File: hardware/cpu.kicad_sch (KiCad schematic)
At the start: 9 parts, among them U1 H3

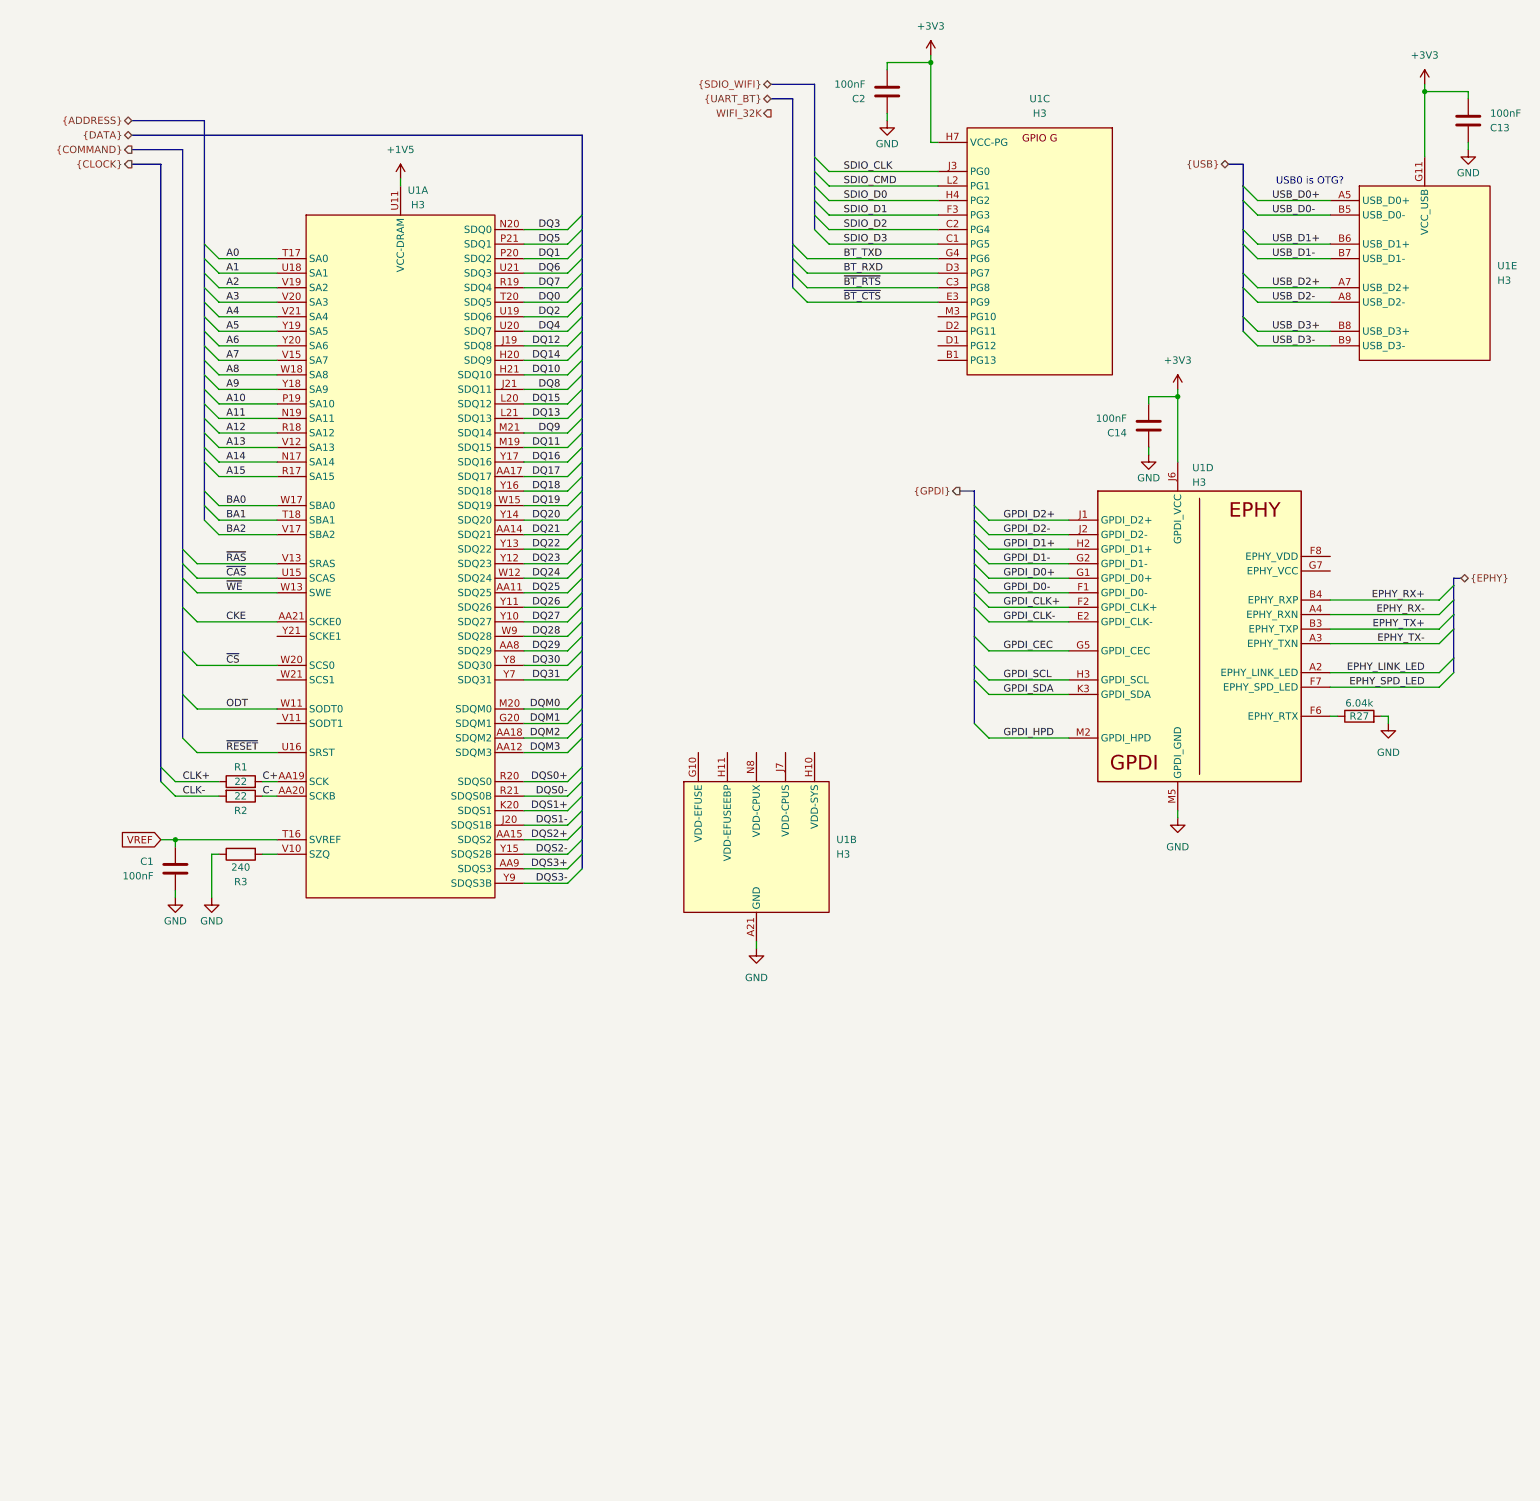
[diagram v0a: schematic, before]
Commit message: Add eMMC and uSD
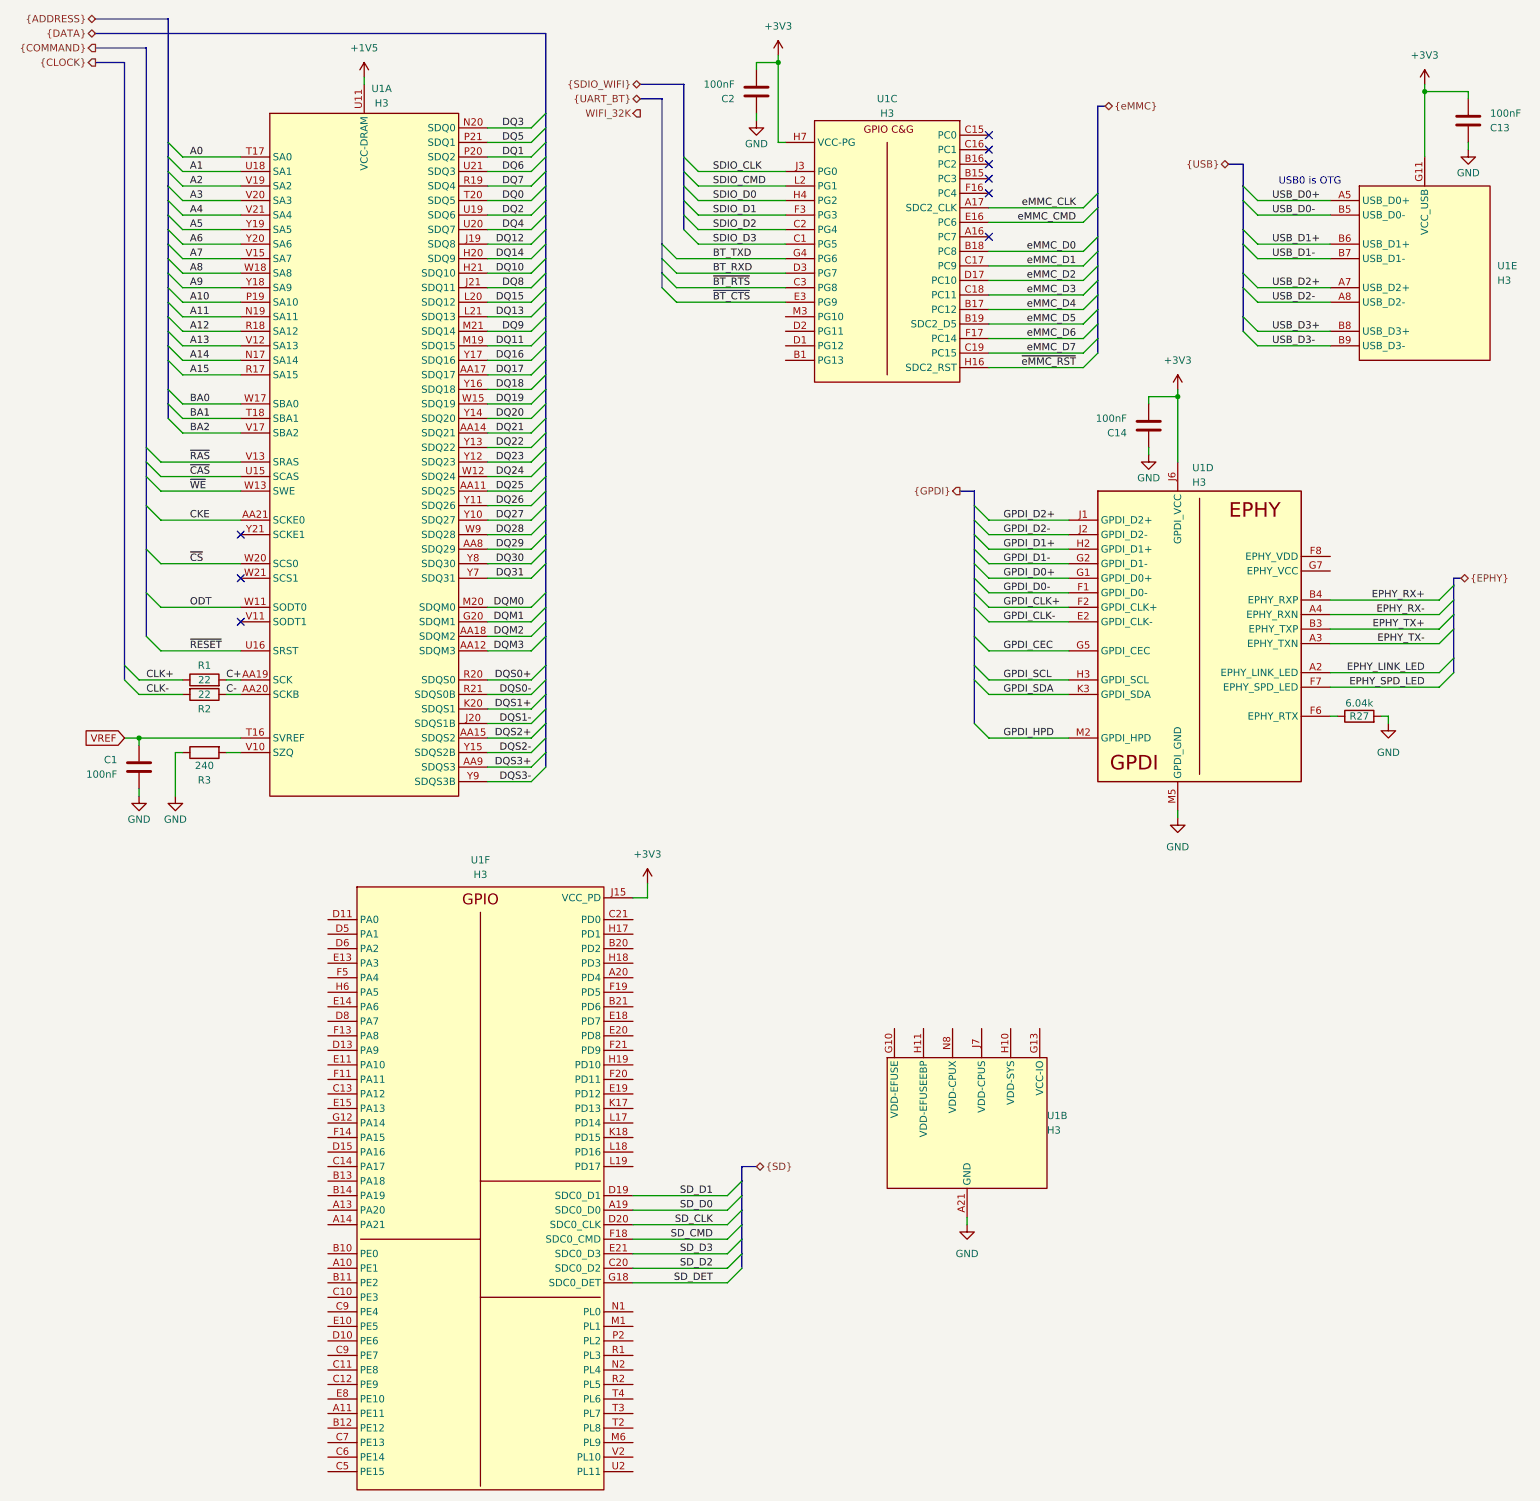
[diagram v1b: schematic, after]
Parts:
- added unit 6 of U1
- U1: LCSC Part # C94644 -> (none)
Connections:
- net +3V3: now also U1.J15 (VCC_PD)
- new net SD_CLK: U1.D20 (PF2)
- new net SD_CMD: U1.F18 (PF3)
- new net SD_D0: U1.A19 (PF1)
- new net SD_D1: U1.D19 (PF0)
- new net SD_D2: U1.C20 (PF5)
- new net SD_D3: U1.E21 (PF4)
- new net SD_DET: U1.G18 (PF6)
- new net VCC-IO: U1.G13 (VCC-IO), U1.G14 (VCC-IO), U1.G15 (VCC-IO), U1.H13 (VCC-IO), U1.H14 (VCC-IO), U1.J14 (VCC-IO)
- new net eMMC_CLK: U1.A17 (PC5)
- new net eMMC_CMD: U1.E16 (PC6)
- new net eMMC_D0: U1.B18 (PC8)
- new net eMMC_D1: U1.C17 (PC9)
- new net eMMC_D2: U1.D17 (PC10)
- new net eMMC_D3: U1.C18 (PC11)
- new net eMMC_D4: U1.B17 (PC12)
- new net eMMC_D5: U1.B19 (PC13)
- new net eMMC_D6: U1.F17 (PC14)
- new net eMMC_D7: U1.C19 (PC15)
- new net ~{eMMC_RST}: U1.H16 (PC16)
- no-connect marks 0 -> 9
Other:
- note added: "USB0 is OTG"
- note removed: "USB0 is OTG?"
- moved on the sheet: C1, C2, R1, R2, R3, U1A
